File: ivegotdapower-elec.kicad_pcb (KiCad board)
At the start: 2 copper layers, 87 x 70 mm, 74 parts, among them J1 Conn_Debug, J10 Conn_+3.3V, J11 Conn_bau, J12 CAN_conn, J13 CAN_conn, J2 Conn_batt, J3 Conn_alim, J4 Conn_TSMR, J5 Conn_POW2, J6 Conn_POW1, J7 Conn_RPi, J8 Conn_+5V, Q1 IRFR5305, Q2 IRFR5305, Q3 BSS138, Q4 MMBT2907A, Q5 MMBT2907A, Q6 MMBT2907A, Q7 MMBT2907A, U1 TCAN332, U10 LD1117S33TR_SOT223, U11 LM358, U6 ACS711xLCTR-12AB, U7 STM32F303K8Tx, U8 LD1117S50TR_SOT223

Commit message: Sérigraphie
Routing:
- net GND: track 618.1 -> 613.9 mm

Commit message: Sérigraphies
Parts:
- moved D15 0.40 mm to (83.1, 117.8), turned to 0 degrees
- moved R24 0.40 mm to (83.2, 117.8)
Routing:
- net GND: track 613.9 -> 606.0 mm
- net Net-(D15-Pad2): track 5.74 -> 0.00 mm
- net /STM32/sense: track 122.0 -> 119.3 mm
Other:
- outline, holes or cut-outs redrawn
- board text added: "BAU"
- board text added: "CAN"
- board text added: "Pow 1"
- board text added: "Pow 2"
- board text added: "Power"
- board text added: "Raspi"
- board text added: "SWD+UART"

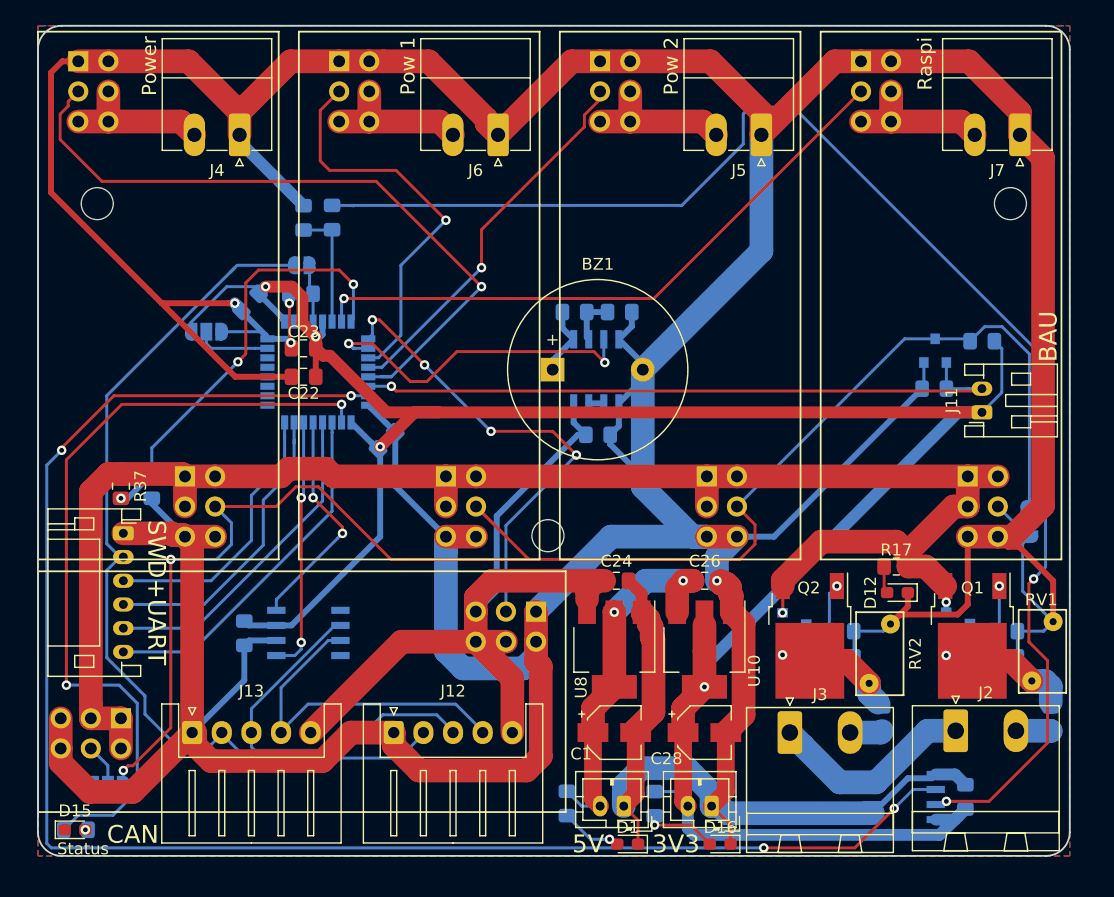
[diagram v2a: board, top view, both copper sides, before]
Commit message: Connect mountholes to GND, silkscreen
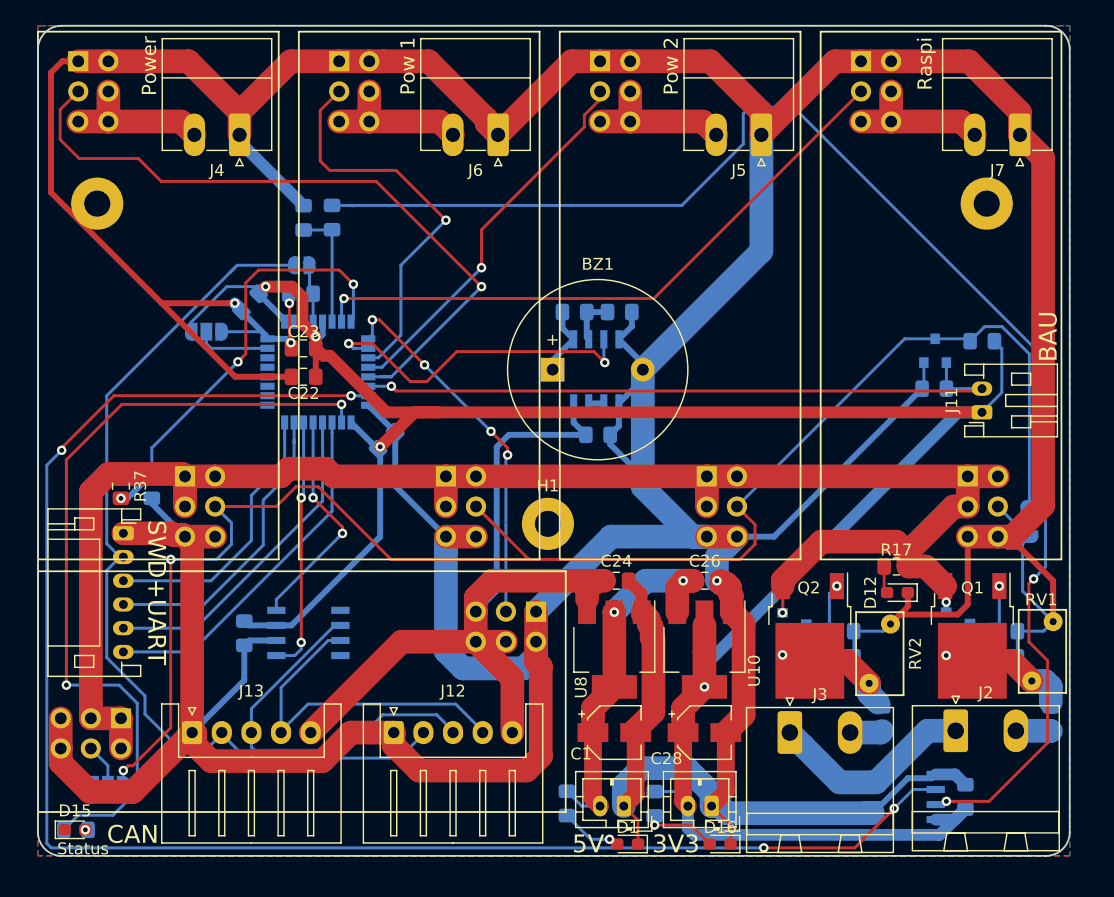
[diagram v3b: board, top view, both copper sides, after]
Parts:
- H1, H2, H3: value MountingHole -> MountingHole_Pad; footprint MountingHole:MountingHole_2.7mm_M2.5 -> MountingHole:MountingHole_2.2mm_M2_Pad
- moved H2 2.00 mm to (160.0, 65.0)
- moved H1 1.00 mm to (123.0, 92.0)
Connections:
- H1 pad 1: (no net) -> GND
- H2 pad 1: (no net) -> GND
- H3 pad 1: (no net) -> GND
- U1 pad 5: (no net) -> Net-(U1-Pad5)
- U1 pad 8: (no net) -> Net-(U1-Pad8)
- U7 pad 2: (no net) -> Net-(U7-Pad2)
- U7 pad 25: (no net) -> Net-(U7-Pad25)
- U7 pad 26: (no net) -> Net-(U7-Pad26)
- U7 pad 27: (no net) -> Net-(U7-Pad27)
- U7 pad 28: (no net) -> Net-(U7-Pad28)
- U7 pad 29: (no net) -> Net-(U7-Pad29)
- U7 pad 3: (no net) -> Net-(U7-Pad3)
- U7 pad 30: (no net) -> Net-(U7-Pad30)
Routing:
- net /buck/Logic_mes: track 39.3 -> 31.4 mm
- net +7.5V: track 71.1 -> 74.5 mm

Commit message: Board cleanup, reorganize
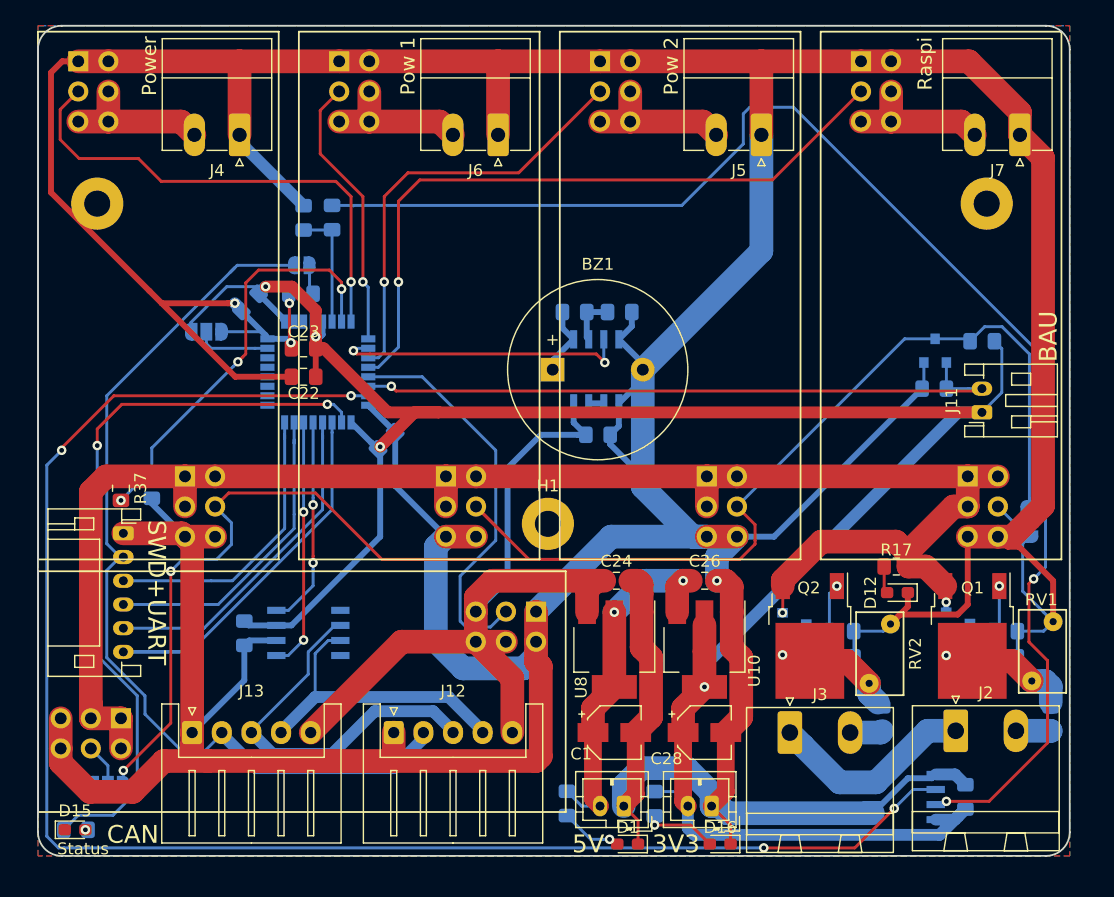
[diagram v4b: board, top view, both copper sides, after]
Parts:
- moved R37 0.17 mm to (87.0, 89.0)
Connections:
- U7 pad 11: /buck/Pow1_mes -> /buck/Pow2_mes
- U7 pad 12: /buck/Pow2_mes -> /buck/RPi_mes
- U7 pad 13: /STM32/TSMR -> /buck/Logic_mes
- U7 pad 7: /buck/RPi_mes -> /STM32/raw
- U7 pad 8: /STM32/raw -> /STM32/TSMR
- U7 pad 9: /buck/Logic_mes -> /buck/Pow1_mes
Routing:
- net /STM32/TSMR: track 59.0 -> 41.8 mm
- net /buck/Pow1_mes: track 34.0 -> 23.2 mm
- net /STM32/TX_1: track 30.0 -> 35.5 mm
- net /buck/RPi_mes: track 52.9 -> 58.4 mm
- net Net-(R24-Pad2): track 67.2 -> 62.1 mm
- net /buck/Pow2_mes: track 32.0 -> 36.5 mm
- net Net-(U11-Pad3): track 28.9 -> 24.9 mm
- net +7.5V: track 74.5 -> 70.7 mm
- net Net-(J12-Pad4): track 29.6 -> 25.9 mm
- net /buck/Logic_mes: track 31.4 -> 33.6 mm, vias 4 -> 0
- net GND: track 606.0 -> 607.5 mm
- net /STM32/CAN_RX: track 19.2 -> 17.7 mm
- net /buck/on-off: track 138.0 -> 136.7 mm
- net /STM32/TCK: track 23.6 -> 24.7 mm
- net /STM32/nrst: track 77.5 -> 78.5 mm
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
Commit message: small cleanup
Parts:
- moved R17 2.39 mm to (150.2, 96.6), turned to 270 degrees
- moved D12 0.53 mm to (153.0, 97.8)
- moved F7 0.22 mm to (151.4, 108.4)
- moved F6 0.05 mm to (165.4, 108.4)
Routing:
- net /buck/power: track 140.6 -> 141.9 mm
- net GND: track 607.5 -> 606.4 mm
- net Net-(F6-Pad1): track 8.84 -> 8.30 mm
- net Net-(F7-Pad1): track 7.72 -> 8.26 mm

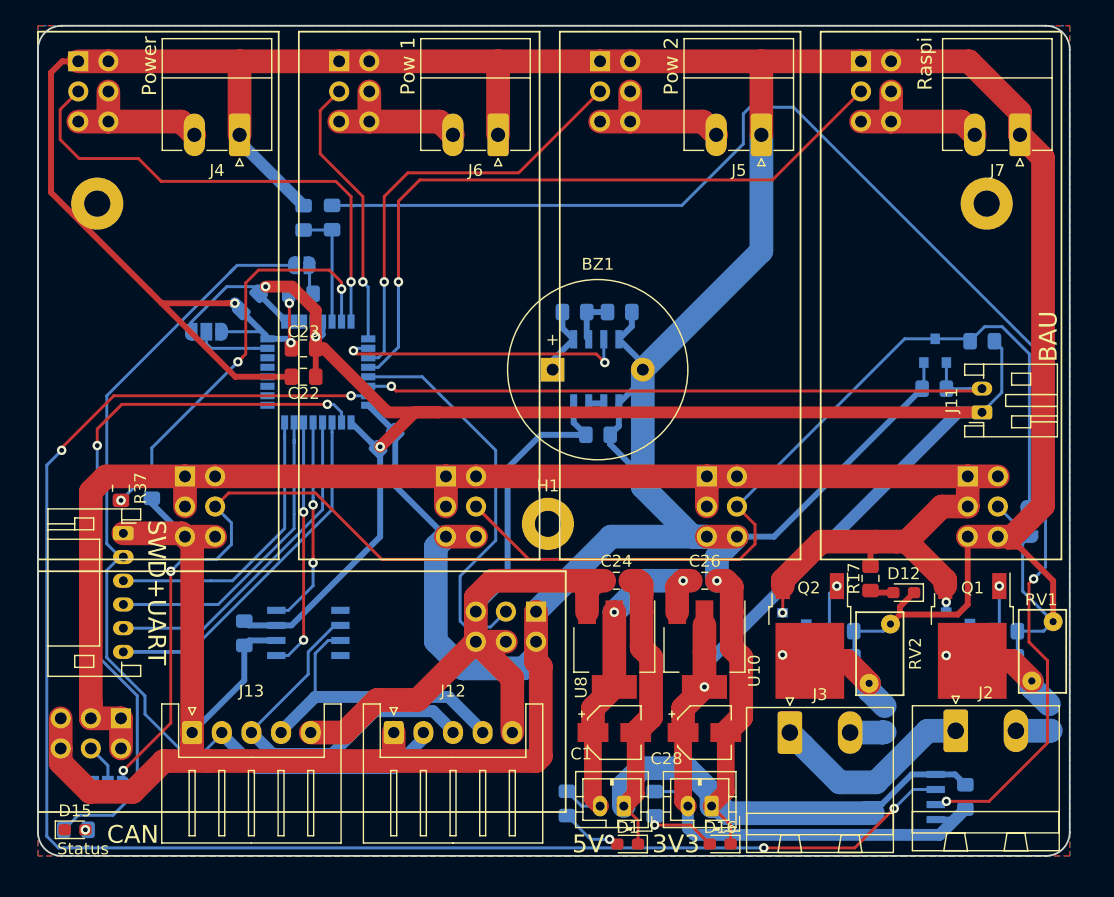
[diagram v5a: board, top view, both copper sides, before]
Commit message: Moved MC connectors
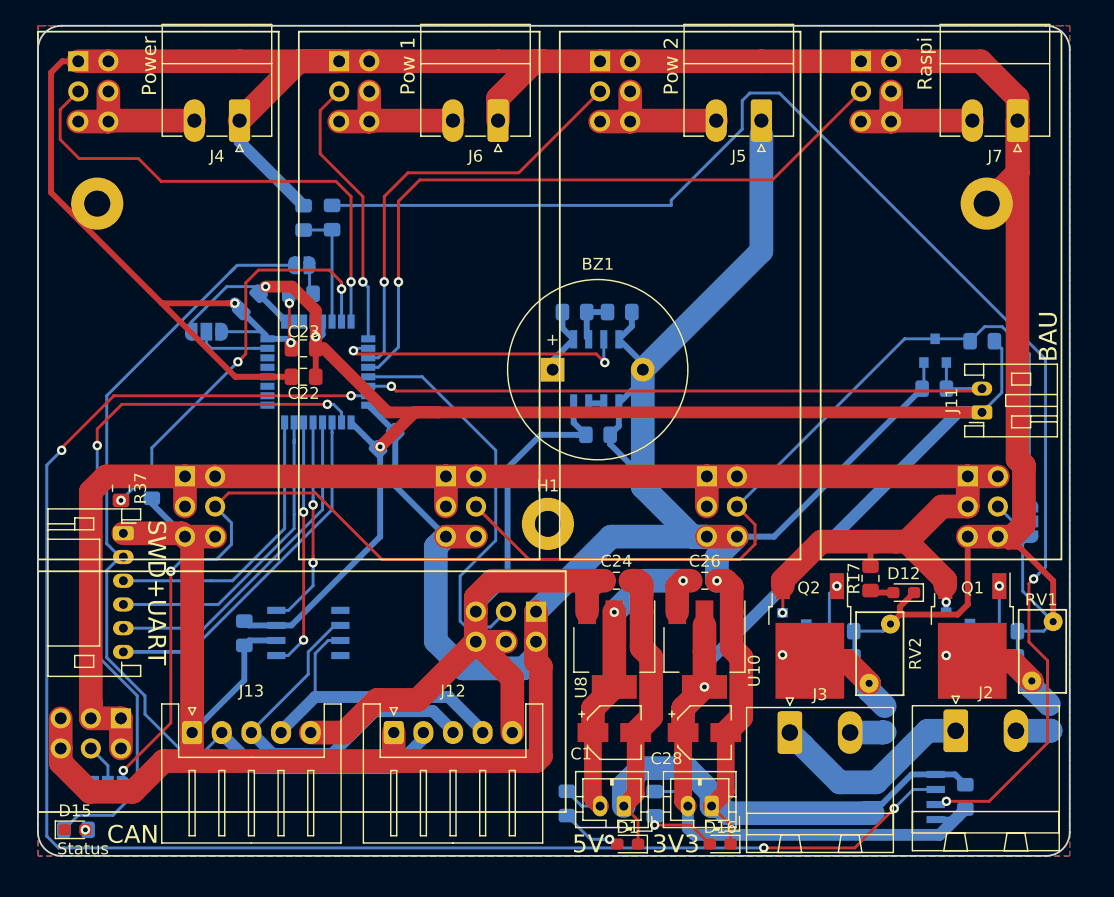
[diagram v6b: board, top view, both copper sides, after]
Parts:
- moved J7 1.22 mm to (162.6, 58.0)
- moved J4 1.20 mm to (97.0, 58.0)
- moved J5 1.20 mm to (141.0, 58.0)
- moved J6 1.20 mm to (118.8, 58.0)
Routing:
- net GND: track 606.4 -> 612.5 mm
- net /STM32/sense: track 119.3 -> 120.4 mm
- net Net-(B1-Pad10): track 12.6 -> 12.0 mm

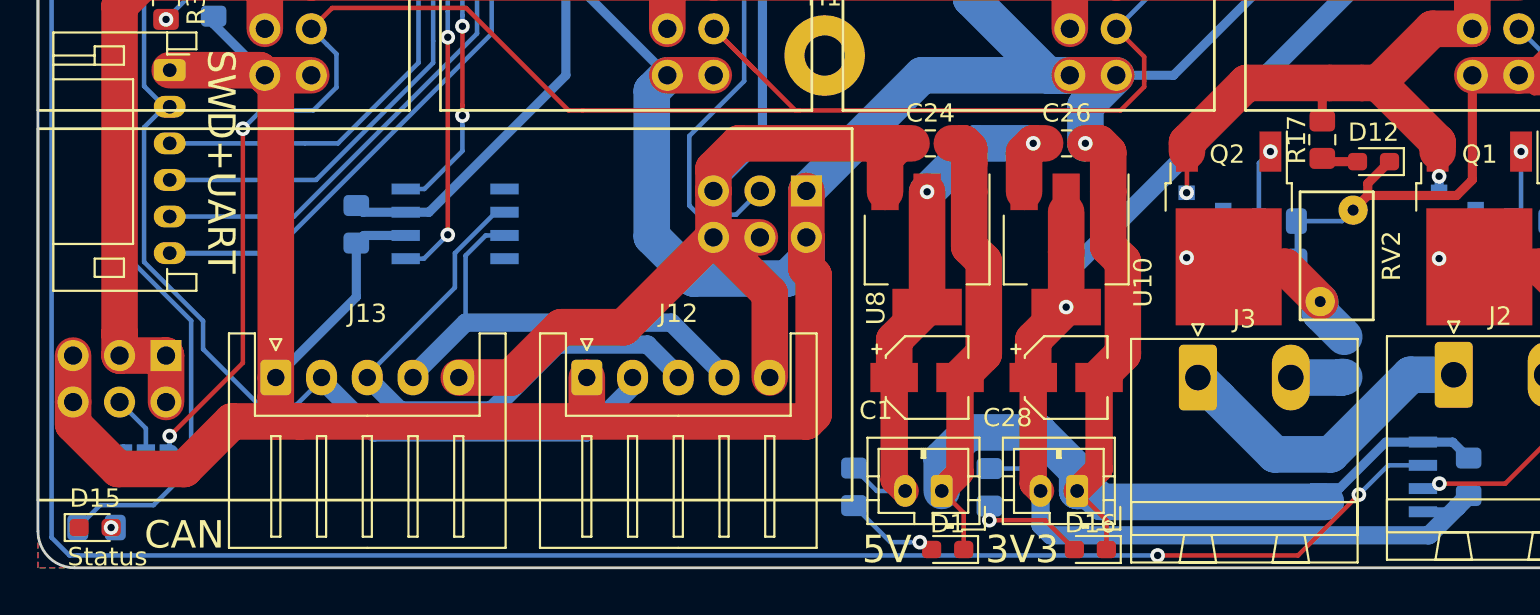
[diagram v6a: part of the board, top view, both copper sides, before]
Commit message: Changed LED footprints
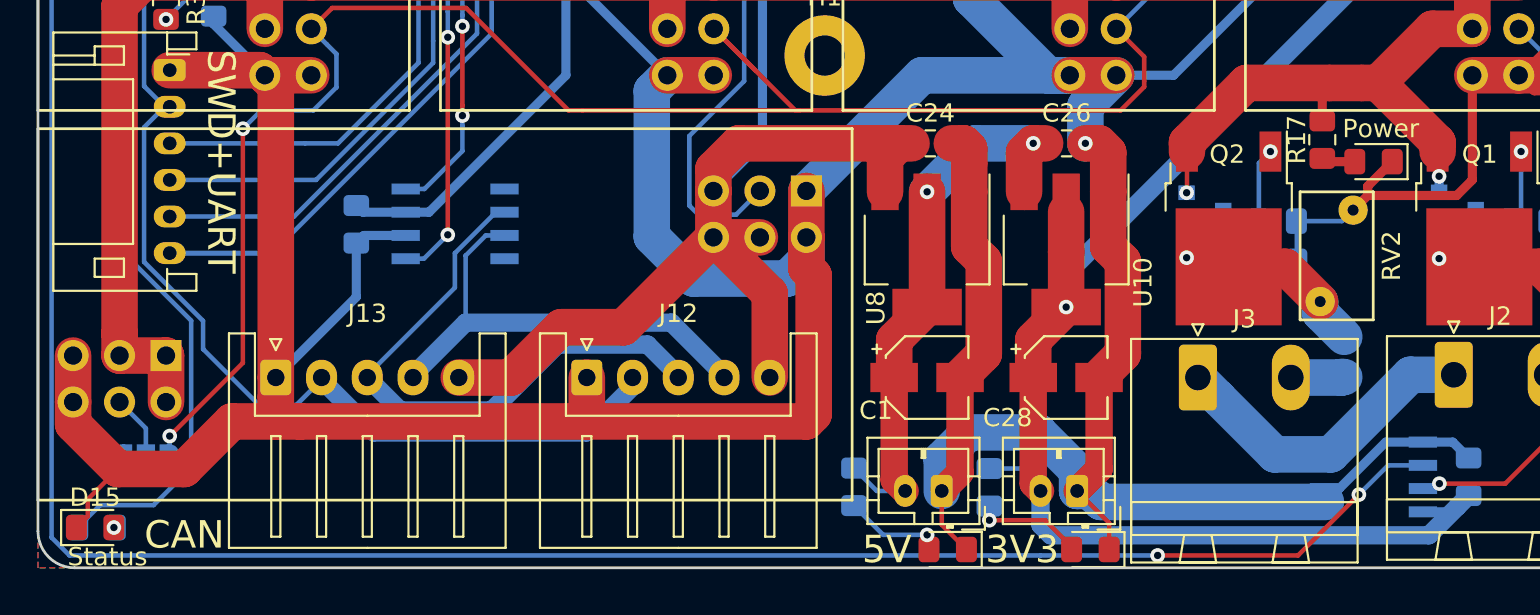
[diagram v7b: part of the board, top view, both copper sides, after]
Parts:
- C16, C25, C26: value C -> 100nF
- D1, D12, D15, D16: footprint LED_SMD:LED_0603_1608Metric_Pad1.05x0.95mm_HandSolder -> LED_SMD:LED_0805_2012Metric_Pad1.15x1.40mm_HandSolder
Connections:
- U1 pad 5: Net-(U1-Pad5) -> (no net)
- U1 pad 8: Net-(U1-Pad8) -> (no net)
- U7 pad 2: Net-(U7-Pad2) -> (no net)
- U7 pad 25: Net-(U7-Pad25) -> (no net)
- U7 pad 26: Net-(U7-Pad26) -> (no net)
- U7 pad 27: Net-(U7-Pad27) -> (no net)
- U7 pad 28: Net-(U7-Pad28) -> (no net)
- U7 pad 29: Net-(U7-Pad29) -> (no net)
- U7 pad 3: Net-(U7-Pad3) -> (no net)
- U7 pad 30: Net-(U7-Pad30) -> (no net)
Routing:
- net GND: track 612.5 -> 616.9 mm

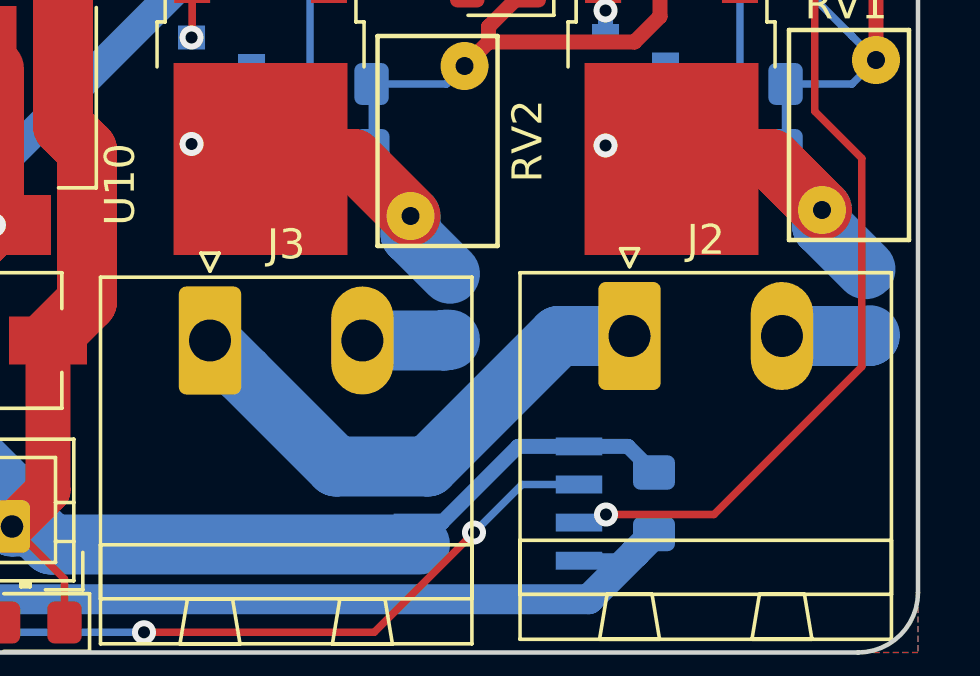
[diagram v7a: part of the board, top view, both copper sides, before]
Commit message: Changed fuse footprint
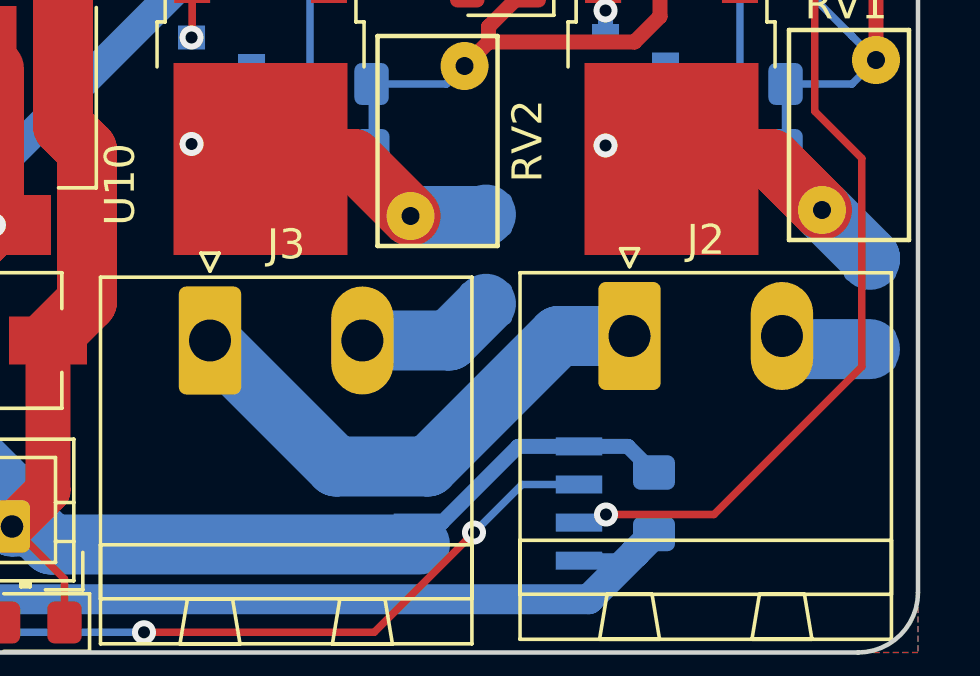
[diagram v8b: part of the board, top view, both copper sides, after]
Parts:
- F6, F7: footprint Fuse:Fuse_0805_2012Metric_Pad1.15x1.40mm_HandSolder -> Fuse:Fuse_1206_3216Metric_Pad1.42x1.75mm_HandSolder
- moved F7 1.93 mm to (152.6, 106.9)
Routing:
- net /power_selection/Valim+: track 2.93 -> 4.63 mm
